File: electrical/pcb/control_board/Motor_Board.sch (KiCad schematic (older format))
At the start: 92 parts, among them J1 XT30-M, J10 Molex_172675-0613, J11 Molex_172675-0613, J12 TSW-104-07-F-T, J13 Molex_172675-0613, J14 Molex_172675-0613, J15 TSW-104-07-F-T, J16 277-11404-ND, J17 277-11404-ND, J18 277-11404-ND, J19 TSW-104-07-F-T, J2 XT30-F, J20 PEC08SAAN, J21 PPTC102LFBN-RC, J3 XT30-F, J4 XT30-F, J5 XT30-M, J6 ED2580-ND, J7 TSW-104-07-F-T, J8 Molex_172675-0613, J9 Molex_172675-0613, Q1 2N3906, T1 test_point, T10 test_point, T11 test_point, T12 test_point, T2 test_point, T3 test_point, T4 test_point, T5 test_point, T6 test_point, T7 test_point, T8 test_point, T9 test_point, U1 INA260, U2 PCA9685, U3 D24V22Fx, U4 D24V150Fx, U5 DC7G3HWA, U7 MIC2937A-3.3WT, y1 rover_silkscreen

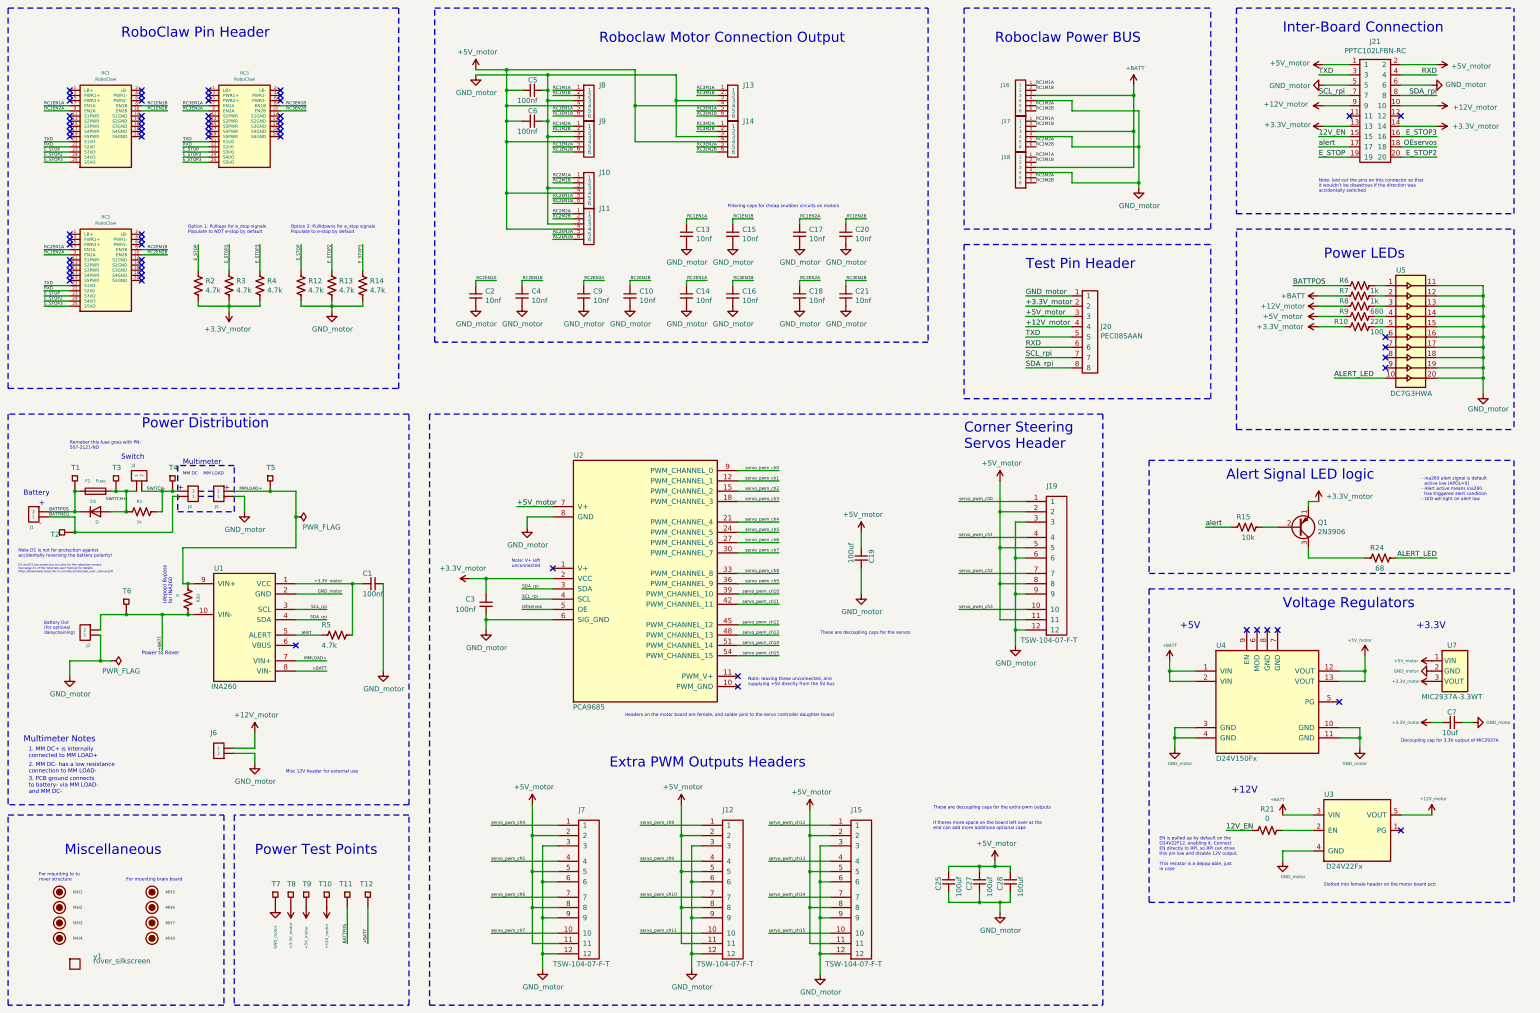
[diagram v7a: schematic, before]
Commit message: Updating annotations
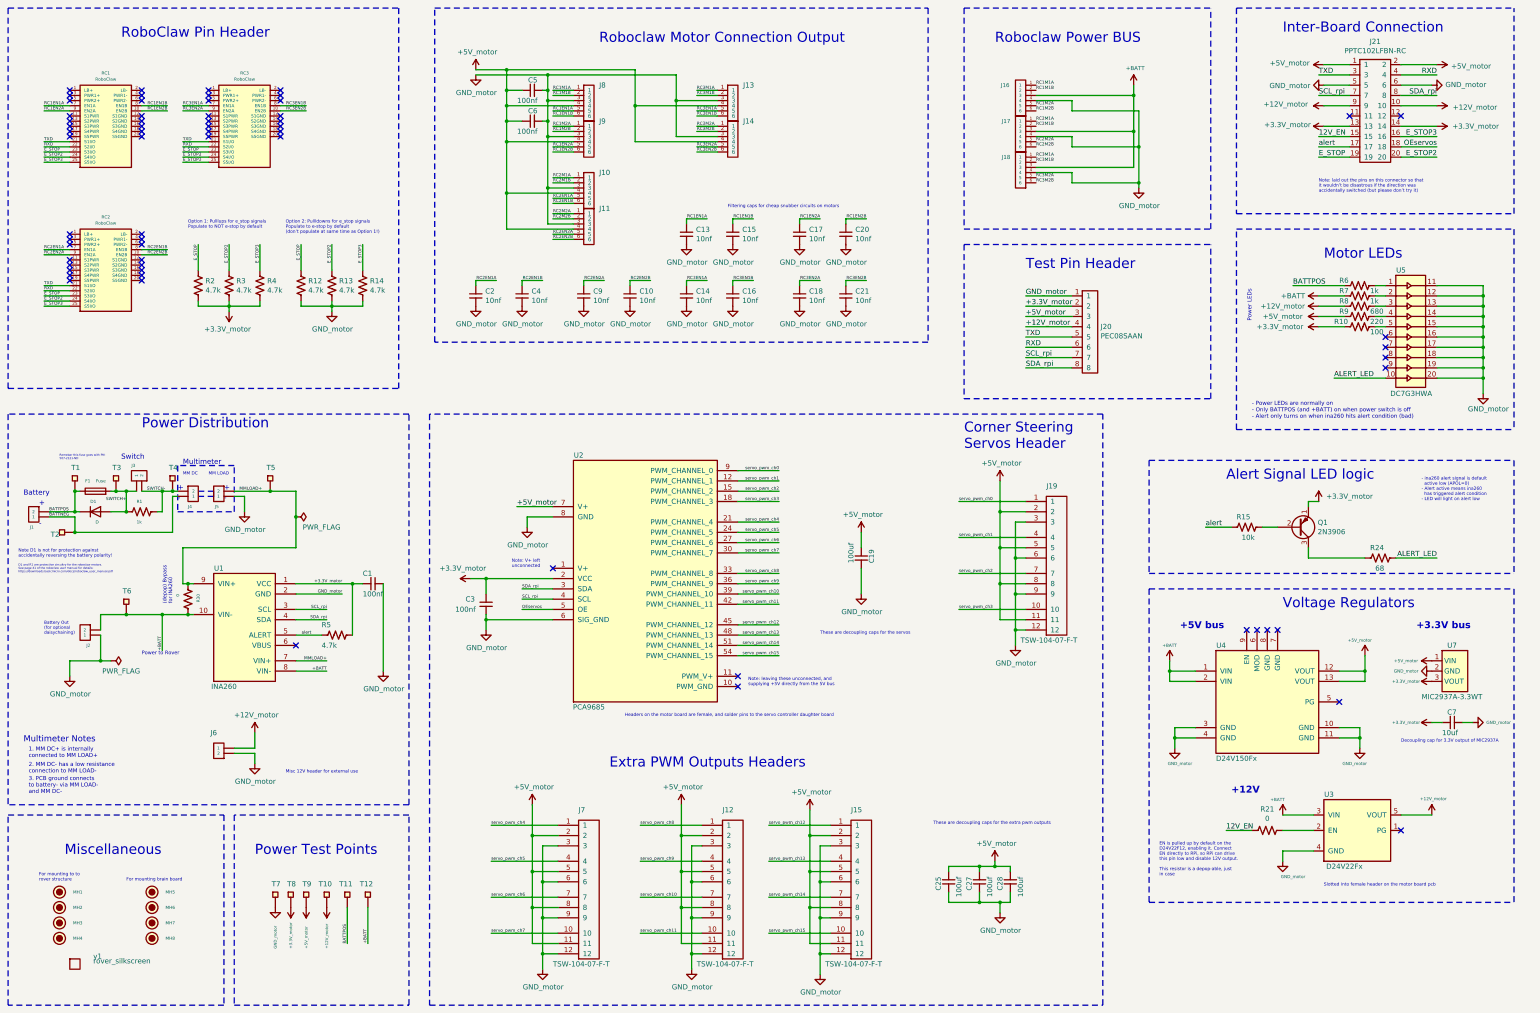
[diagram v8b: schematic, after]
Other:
- note added: "+3.3V bus"
- note added: "+5V bus"
- note added: "- Power LEDs are normally on\n- Only BATTPOS (and +BATT) on when power switch is off\n- Alert only turns on when ina260 hits alert condition (bad)"
- note added: "Motor LEDs"
- note added: "Note: laid out the pins on this connector so that \nit wouldn’t be disastrous if the direction was \naccidentally switched (but please don’t try it)"
- note added: "Option 2: Pullldowns for e_stop signals\nPopulate to e-stop by default\n(don’t populate at same time as Option 1!)"
- note removed: "+3.3V\n"
- note removed: "+5V\n"
- note removed: "If theres more space on the board left over at the \nend can add more additiona optional caps"
- note removed: "Note: laid out the pins on this connector so that \nit wouldn’t be disastrous if the direction was \naccidentally switched"
- note removed: "Option 2: Pullldowns for e_stop signals\nPopulate to e-stop by default"
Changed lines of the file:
@@
 Text Label 3450 3250 3    30   ~ 0
 E_STOP3
-Text Notes 2750 3150 0    31   ~ 0
+Text Notes 2750 3100 0    31   ~ 0
 Option 1: Pulllups for e_stop signals\nPopulate to NOT e-stop by default
 $Comp
@@
 $EndComp
 Text Notes 13800 3400 0    98   ~ 0
-Power LEDs
+Motor LEDs
 Text Label 13500 3650 0    50   ~ 0
 BATTPOS
@@
 	1    0    0    -1
 $EndComp
-Text Notes 13800 9500 0    31   ~ 0
-Slotted into female header on the motor board pcb
 Text Notes 8000 2900 0    31   ~ 0
 Filtering caps for cheap snubber circuits on motors
@@
 Text Notes 8200 7550 0    31   ~ 0
 Note: leaving these unconnected, and \nsupplying +5V directly from the 5V bus
-Text Notes 10000 8950 0    31   ~ 0
-If theres more space on the board left over at the \nend can add more additiona optional caps
 Wire Wire Line
 	5750 3600 5550 3600
@@
 Text Notes 7000 7850 0    31   ~ 0
 Headers on the motor board are female, and solder pins to the servo controller daughter board
-Text Notes 10000 8750 0    31   ~ 0
-These are decoupling caps for the extra pwm outputs
 Text Notes 8900 7050 0    31   ~ 0
 These are decoupling caps for the servos
@@
 NoConn ~ 13250 7000
 NoConn ~ 13350 7000
-Text Notes 12200 9350 0    31   ~ 0
+Text Notes 12200 9400 0    31   ~ 0
 EN is pulled up by default on the \nD24V22F12, enabling it. Connect \nEN directly to RPi, so RPi can drive \nthis pin low and disable 12V output. \n\nThis resistor is a depop-able, just \nin case
 Text Notes 13750 2750 0    31   ~ 0
-Note: laid out the pins on this connector so that \nit wouldn’t be disastrous if the direction was \naccidentally switched
+Note: laid out the pins on this connector so that \nit wouldn’t be disastrous if the direction was \naccidentally switched (but please don’t try it)
 Text Label 1400 5850 0    30   ~ 0
 BATTPOS
@@
 Text Notes 2650 5650 0    50   ~ 0
 +
-Text Notes 2900 5500 0    30   ~ 0
+Text Notes 2950 5500 0    30   ~ 0
 MM LOAD
 Text Notes 2700 5500 0    30   ~ 0
@@
 	0    1    1    0
 $EndComp
-Text Notes 1600 5250 0    31   ~ 0
+Text Notes 1500 5350 0    20   ~ 0
 Remeber this fuse goes with PN:\n507-2121-ND
 Wire Wire Line
@@
 Wire Wire Line
 	4150 3900 4150 3850
-Text Notes 3750 3150 0    31   ~ 0
-Option 2: Pullldowns for e_stop signals\nPopulate to e-stop by default
+Text Notes 3700 3150 0    31   ~ 0
+Option 2: Pullldowns for e_stop signals\nPopulate to e-stop by default\n(don’t populate at same time as Option 1!)
 $Comp
 L JPL_Robotics_Lib:GND_motor #PWR066
@@
 Wire Notes Line
 	12100 6600 12100 9650
-Text Notes 12400 7000 0    67   ~ 0
-+5V\n
-Text Notes 12900 8600 0    67   ~ 0
+Text Notes 12400 7000 0    67   ~ 13
++5V bus
+Text Notes 12900 8600 0    67   ~ 13
 +12V\n
-Text Notes 14700 7000 0    67   ~ 0
-+3.3V\n
+Text Notes 14700 7000 0    67   ~ 13
++3.3V bus
 $Comp
 L JPL_Robotics_Lib:+5V_motor #PWR0105
@@
 Wire Wire Line
 	12650 6000 12900 6000
+Text Notes 13100 4950 0    39   ~ 0
+- Power LEDs are normally on\n- Only BATTPOS (and +BATT) on when power switch is off\n- Alert only turns on when ina260 hits alert condition (bad)
+Text Notes 13100 4000 1    39   ~ 0
+Power LEDs
+Text Notes 10000 8900 0    31   ~ 0
+These are decoupling caps for the extra pwm outputs
+Text Notes 13800 9500 0    31   ~ 0
+Slotted into female header on the motor board pcb
 $EndSCHEMATC
